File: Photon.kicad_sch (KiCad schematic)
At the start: 55 parts, among them J1 USB_C_Receptacle_USB2.0_14P, Q1 IRLML6402, Q2 IRLML6402, SW1 TS-1088-AR02016, U1 ATtiny13A-S, U2 RT8059GJ5, U3 TP4056, U4 BCR421UW6-7, U5 DW01A, U6 FS8205A, U7 BCR421UW6-7

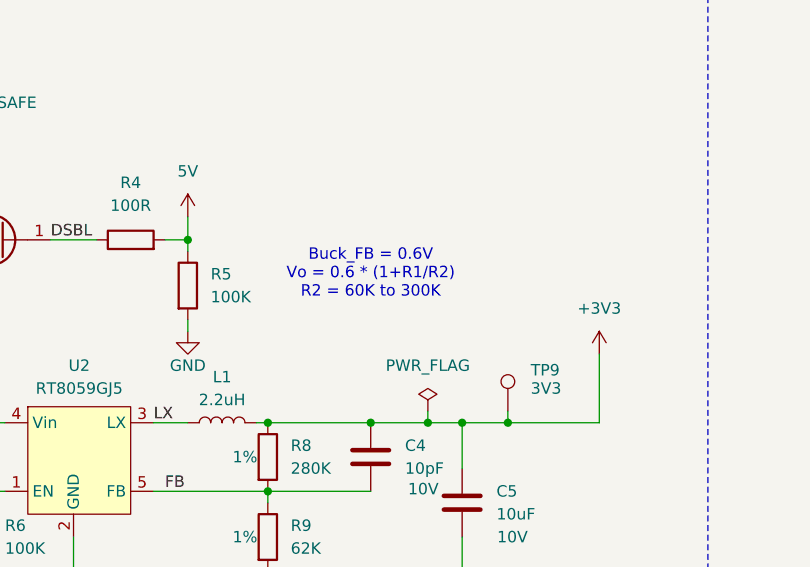
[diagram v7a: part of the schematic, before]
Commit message: made RT805 smaller footprint, moved few parts around and center tp4056 more over battery through holes
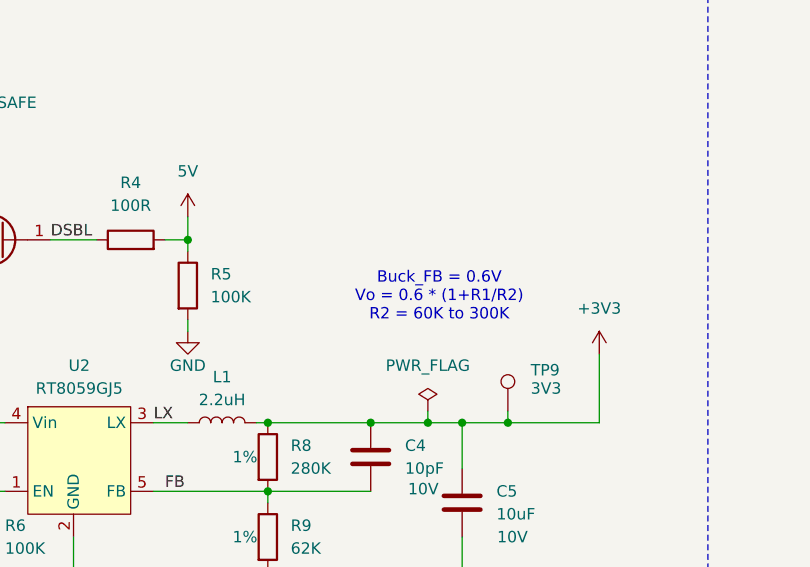
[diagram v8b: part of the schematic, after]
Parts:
- U2: footprint Package_TO_SOT_SMD:SOT-23-5_HandSoldering -> Package_TO_SOT_SMD:SOT-23-5
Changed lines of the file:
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@@
 	(text "Buck_FB = 0.6V\nVo = 0.6 * (1+R1/R2) \nR2 = 60K to 300K"
 		(exclude_from_sim no)
-		(at 215.9 187.96 0)
+		(at 223.52 190.5 0)
 		(effects
 			(font
@@
 			)
 		)
-		(property "Footprint" "Package_TO_SOT_SMD:SOT-23-5_HandSoldering"
+		(property "Footprint" "Package_TO_SOT_SMD:SOT-23-5"
 			(at 182.88 207.01 0)
 			(effects
